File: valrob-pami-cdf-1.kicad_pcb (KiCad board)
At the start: 4 copper layers, 58 x 50 mm, 139 parts, among them J1 Conn_01x04, J2 USB_C_Receptacle_USB2.0_14P, J3 Conn_01x02, J4 Conn_01x04_Pin, J5 Conn_01x06, M1 Motor_Servo, M2 Stepper_Motor_bipolar, M3 Stepper_Motor_bipolar, Q1 Q_NMOS, Q2 Q_NMOS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

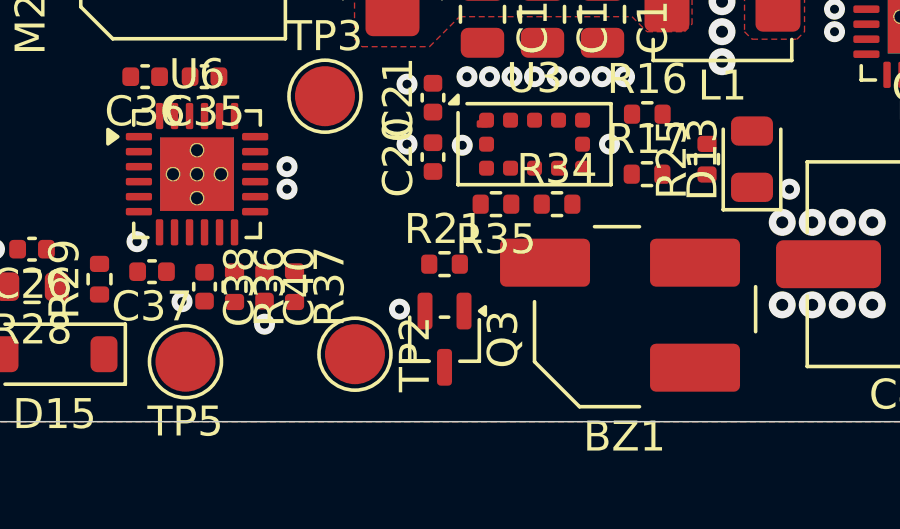
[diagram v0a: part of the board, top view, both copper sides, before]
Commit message: pcb: add buzzer routing
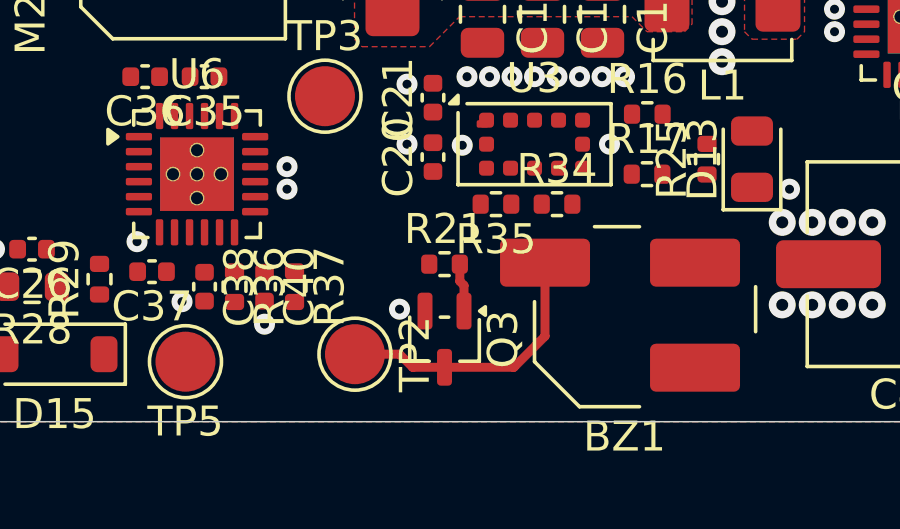
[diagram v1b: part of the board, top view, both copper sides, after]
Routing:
- net Net-(BZ1--): track 0.00 -> 9.40 mm
- net Net-(Q3-G): track 0.00 -> 1.62 mm
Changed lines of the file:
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@@
 		(net 1)
+	)
+	(segment
+		(start 154.8125 121.1875)
+		(end 155.85 120.15)
+		(width 0.3)
+		(layer "F.Cu")
+		(net 3)
+	)
+	(segment
+		(start 155.85 120.15)
+		(end 155.85 117.7)
+		(width 0.3)
+		(layer "F.Cu")
+		(net 3)
+	)
+	(segment
+		(start 151.4375 121.1875)
+		(end 151 120.75)
+		(width 0.3)
+		(layer "F.Cu")
+		(net 3)
+	)
+	(segment
+		(start 151 120.75)
+		(end 149.515 120.75)
+		(width 0.3)
+		(layer "F.Cu")
+		(net 3)
+	)
+	(segment
+		(start 152.5 121.1875)
+		(end 151.4375 121.1875)
+		(width 0.3)
+		(layer "F.Cu")
+		(net 3)
+	)
+	(segment
+		(start 152.5 121.1875)
+		(end 154.8125 121.1875)
+		(width 0.3)
+		(layer "F.Cu")
+		(net 3)
 	)
 	(via
@@
 	)
 	(segment
+		(start 153.01 118.318834)
+		(end 153.15 118.458834)
+		(width 0.3)
+		(layer "F.Cu")
+		(net 66)
+	)
+	(segment
+		(start 153.15 118.458834)
+		(end 153.15 119.3125)
+		(width 0.3)
+		(layer "F.Cu")
+		(net 66)
+	)
+	(segment
+		(start 153.01 117.75)
+		(end 153.01 118.318834)
+		(width 0.3)
+		(layer "F.Cu")
+		(net 66)
+	)
+	(segment

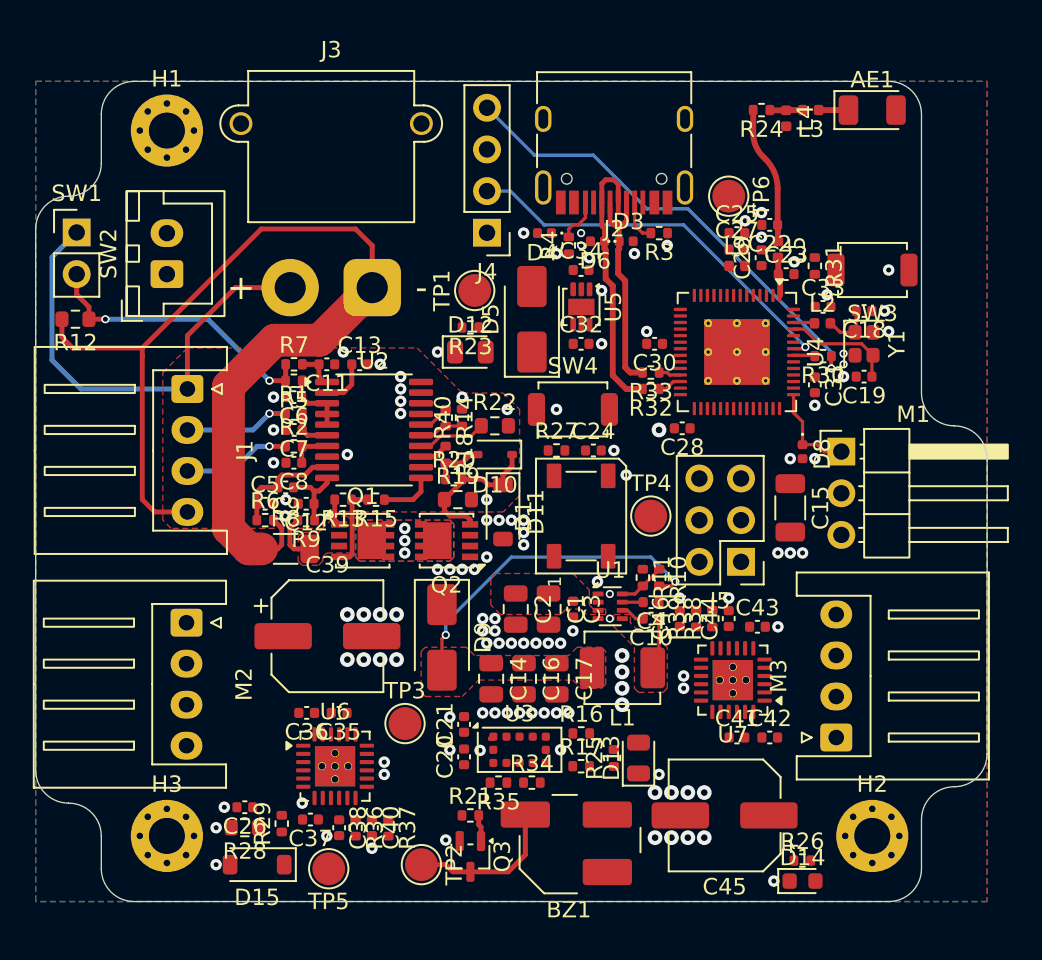
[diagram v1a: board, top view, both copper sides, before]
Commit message: pcb: add local stepper drivers routing
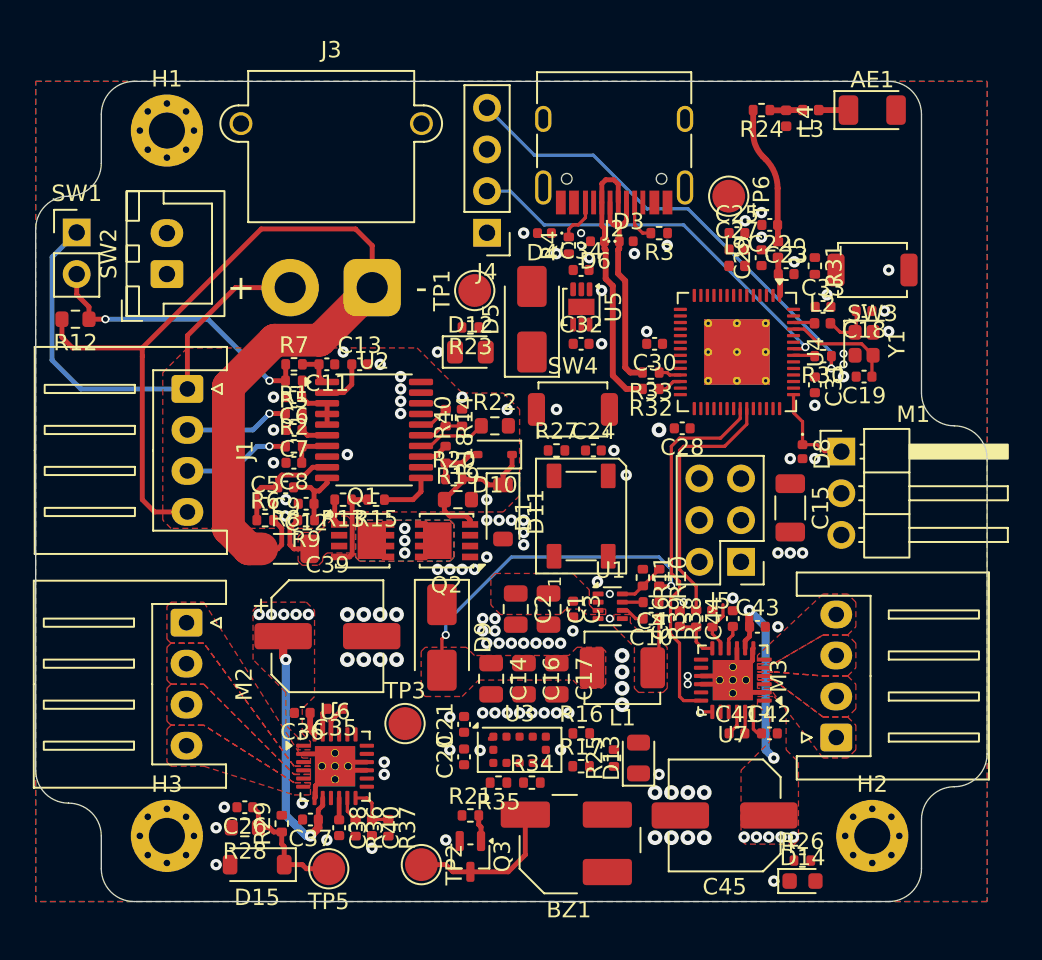
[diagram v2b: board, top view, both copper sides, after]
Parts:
- removed TP4: TestPoint, TestPoint:TestPoint_Pad_D2.0mm
- moved C35 0.35 mm to (144.2, 111.2)
- moved C36 0.27 mm to (142.2, 111.5)
- moved C42 0.25 mm to (170.7, 112.8)
- moved C41 0.25 mm to (168.8, 112.8)
- moved C44 0.25 mm to (168.5, 105.8)
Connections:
- R34 pad 2: +3V3 -> unconnected-(R34-Pad2)
- U4 pad 10: /~{FAULT_1} -> unconnected-(U4-GPIO5/ADC1_CH4-Pad10)
- U4 pad 11: unconnected-(U4-GPIO6/ADC1_CH5-Pad11) -> /~{FAULT_1}
- U4 pad 14: /VPWM_2 -> unconnected-(U4-GPIO9/ADC1_CH8-Pad14)
- U4 pad 17: /STEP_2 -> unconnected-(U4-GPIO12/ADC2_CH1-Pad17)
- U4 pad 23: /~{FAULT_2} -> unconnected-(U4-GPIO17/ADC2_CH6-Pad23)
- U4 pad 36: /SCL -> /STEP_2
- U4 pad 37: /SDA -> /VPWM_2
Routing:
- net +BATT: track 28.1 -> 55.8 mm, vias 0 -> 14
- net /STEP_2: track 0.00 -> 22.8 mm
- net GND: track 0.00 -> 17.2 mm
- net /VPWM_2: track 0.00 -> 15.9 mm
- net /Vsense: track 0.00 -> 7.80 mm
- net Net-(U6-VREF): track 0.00 -> 3.16 mm
- net /~{FAULT_2}: track 0.00 -> 3.14 mm
- net Net-(U7-VREF): track 0.00 -> 3.07 mm
- net Net-(U6-CPL): track 0.00 -> 1.86 mm
- net Net-(U6-CPH): track 0.00 -> 1.67 mm
- net Net-(U7-CPL): track 0.00 -> 1.51 mm
- net /~{FAULT_1}: track 0.00 -> 1.51 mm
- net Net-(U7-DVDD): track 0.00 -> 1.44 mm
- net Net-(U7-VCP): track 0.00 -> 1.42 mm
- net Net-(U6-VCP): track 0.00 -> 1.42 mm
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- added copper zone on F.Cu, net Net-(M2--)
- added copper zone on F.Cu, net Net-(M3--)
- added copper zone on F.Cu, net Net-(U6-AOUT2)
- added copper zone on F.Cu, net Net-(U6-BOUT1)
- added copper zone on F.Cu, net Net-(U6-BOUT2)
- added copper zone on F.Cu, net Net-(U7-AOUT2)
- added copper zone on F.Cu, net Net-(U7-BOUT1)
- added copper zone on F.Cu, net Net-(U7-BOUT2)

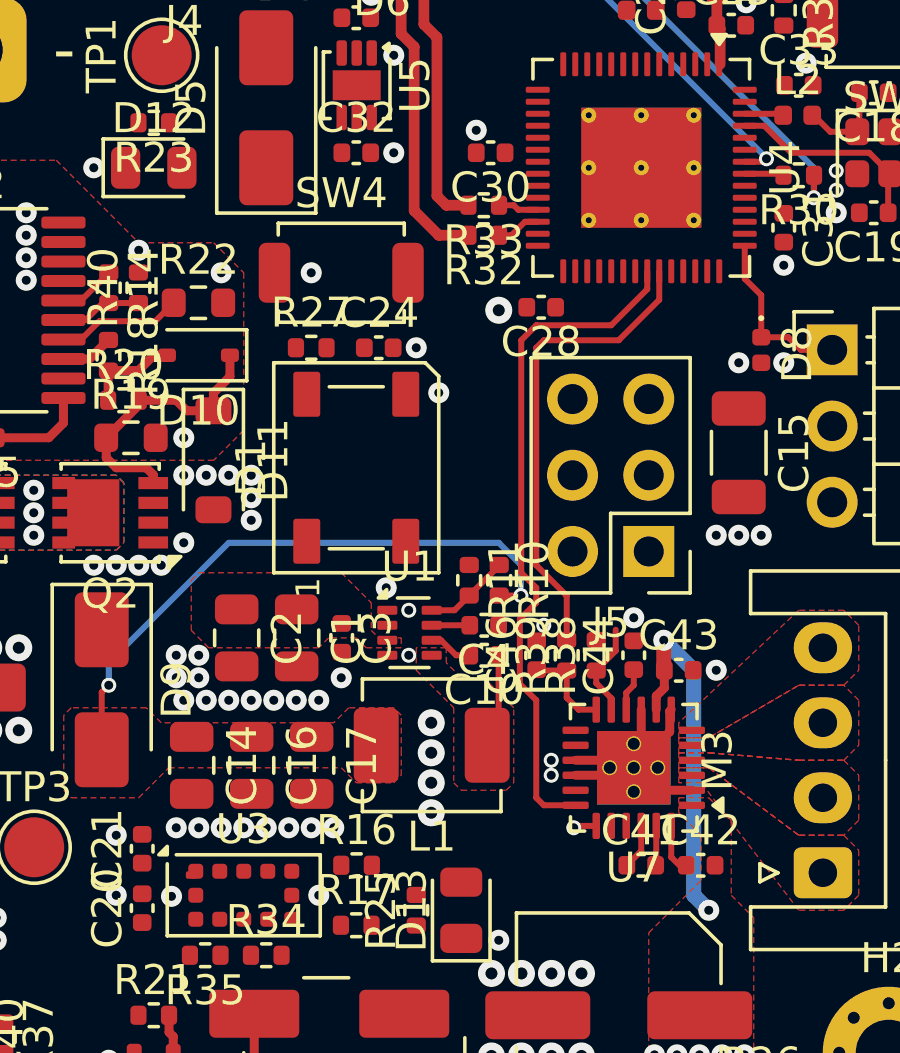
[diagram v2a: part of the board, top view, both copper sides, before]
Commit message: pcb: add right stepper driver routing
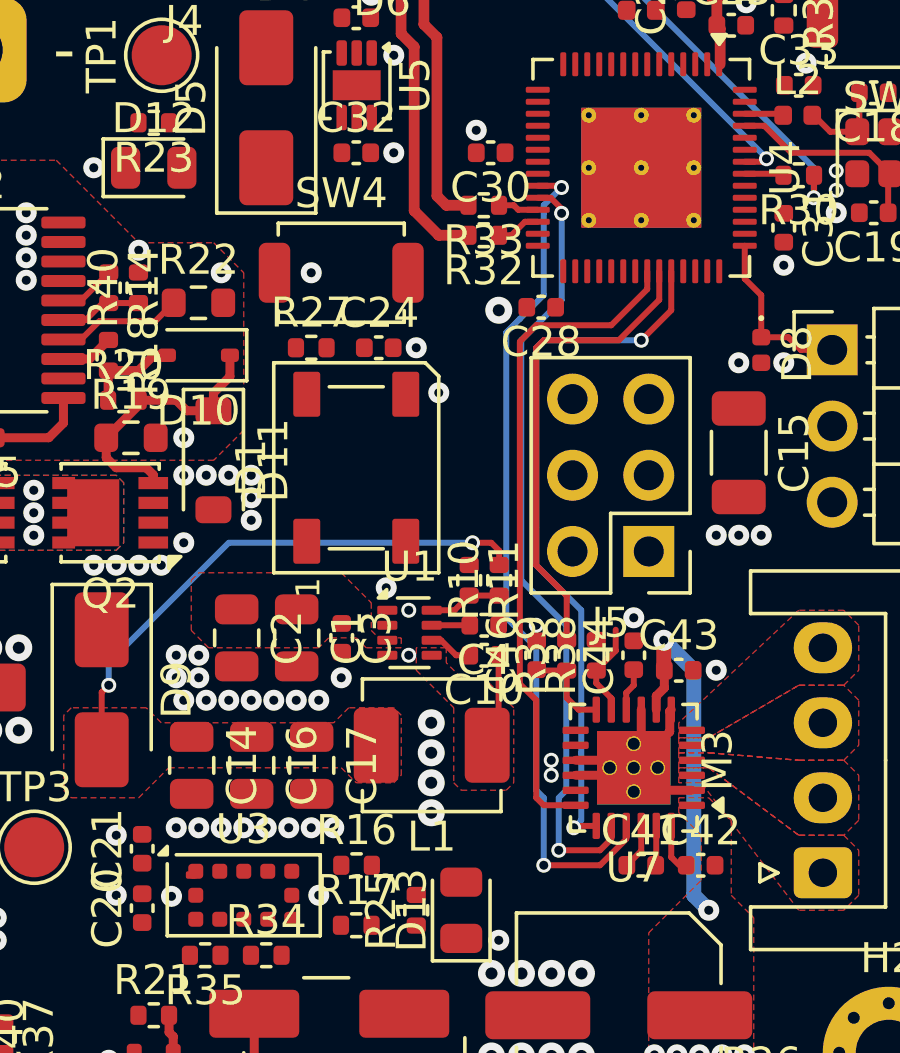
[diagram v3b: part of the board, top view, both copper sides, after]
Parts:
- turned R10 to 90 degrees
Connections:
- U4 pad 16: /DIR_2 -> unconnected-(U4-GPIO11/ADC2_CH0-Pad16)
- U4 pad 18: /EN_2 -> unconnected-(U4-GPIO13/ADC2_CH2-Pad18)
- U4 pad 19: /~{SLEEP_2} -> unconnected-(U4-GPIO14/ADC2_CH3-Pad19)
- U4 pad 23: unconnected-(U4-GPIO17/ADC2_CH6-Pad23) -> /~{SLEEP_2}
- U4 pad 24: /BUZZER -> /EN_2
- U4 pad 38: unconnected-(U4-GPIO33-Pad38) -> /DIR_2
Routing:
- net /~{SLEEP_2}: track 0.00 -> 28.2 mm, vias 0 -> 2
- net /EN_2: track 0.00 -> 26.0 mm, vias 0 -> 2
- net /DIR_2: track 0.78 -> 23.8 mm, vias 1 -> 2
- net +5V: track 20.4 -> 18.3 mm
